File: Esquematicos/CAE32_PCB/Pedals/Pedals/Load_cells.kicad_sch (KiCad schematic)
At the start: 51 parts, among them J17 Conn_01x07_Female, J18 Conn_01x07_Female, J19 Conn_01x07_Female, Q1 MMBT3906, Q2 MMBT3906, Q3 MMBT3906, U5 HX711, U6 HX711, U7 HX711

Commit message: update: Componentes acomodados en la PCB
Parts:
- J18: renamed from J17; value Conn_01x07_Female -> LC_2
- J19: renamed from J18; value Conn_01x07_Female -> LD_1
- J20: renamed from J19; value Conn_01x07_Female -> LC_3
- R10, R11, R12, R13, R14, R15, R16, R17, R18, R19, R20, R6, R7, R8, R9: footprint Resistor_SMD:R_0805_2012Metric_Pad1.20x1.40mm_HandSolder -> Resistor_SMD:R_0603_1608Metric_Pad0.98x0.95mm_HandSolder
- renumbered C23 to C15, C24 to C16, C25 to C17, C26 to C18, C15 to C19, C27 to C20, C28 to C21, C16 to C22, C17 to C23, C18 to C24, C19 to C25, C20 to C26, C21 to C27, C22 to C28, C33 to C29, C34 to C30, C29 to C31, C35 to C32, C30 to C33, C31 to C34, C32 to C35
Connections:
- net B2+: no longer J20.2 (Pin_2)
- net B3+: now also J20.2 (Pin_2)
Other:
- moved on the sheet: C15, C16, C17, C18, C19, C20, C21, C23, C25, C27, C29, C30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

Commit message: update: se agrega el consumo de corriente a los IC's ademas de agregar el URL y numero de parte de los componentes de LCSC en kicad
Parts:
- C15, C16, C17, C18, C19, C22, C23, C24, C27, C28, C29, C30, C31, C33, C35: value 0u1 -> 100n; LCSC_PART (none) -> c1591
- C20, C21, C25, C26, C32, C34: LCSC_PART (none) -> C1691
- J18, J20: LCSC_PART (none) -> C2832270
- J19: value LD_1 -> LC_1; LCSC_PART (none) -> C2832270
- L1, L2, L3: LCSC_PART (none) -> C84474
- R10, R12, R18: LCSC_PART (none) -> C4184
- R11, R13, R19: LCSC_PART (none) -> C114637
- R14, R15, R20: LCSC_PART (none) -> C25804
- R16, R17, R6, R7, R8, R9: LCSC_PART (none) -> C22775
- U5, U6, U7: LCSC_PART (none) -> C43656
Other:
- note added: "ANALOG SUPPLY CURRENT: 1400uA DIGITAL SUPPLY CURRENT: 100uA"
- note added: "HX711"
- title: (none) -> CAE32 pedals

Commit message: Update: esquematicos de PCB, reorganizando elementos para hacer mas compacta la pcb, ademas de agregar serigrafia e imagenes de la PCB
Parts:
- added TP4, TP5, TP6, TP7: TestPoint, TestPoint:TestPoint_Pad_D1.0mm, symbol Connector:TestPoint
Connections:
- net DOUT_1: now also TP5.1
- net DOUT_2: now also TP4.1
- net DOUT_3: now also TP7.1
- net PD_SCK: now also TP6.1
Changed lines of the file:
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@@
   (junction (at 71.12 123.19) (diameter 0) (color 0 0 0 0)
   )
+  (junction (at 118.745 46.355) (diameter 0) (color 0 0 0 0)
+  )
   (junction (at 195.58 87.63) (diameter 0) (color 0 0 0 0)
   )
@@
   (junction (at 73.025 34.925) (diameter 0) (color 0 0 0 0)
   )
+  (junction (at 133.985 48.895) (diameter 0) (color 0 0 0 0)
+  )
+  (junction (at 258.445 99.06) (diameter 0) (color 0 0 0 0)
+  )
   (junction (at 45.72 123.19) (diameter 0) (color 0 0 0 0)
   )
@@
   )
   (junction (at 71.12 132.08) (diameter 0) (color 0 0 0 0)
+  )
+  (junction (at 117.475 134.62) (diameter 0) (color 0 0 0 0)
   )
   (junction (at 51.435 130.81) (diameter 0) (color 0 0 0 0)
@@
     (stroke (width 0) (type default) (color 0 0 0 0))
   )
+  (wire (pts (xy 264.16 99.06) (xy 258.445 99.06))
+    (stroke (width 0) (type default) (color 0 0 0 0))
+  )
   (wire (pts (xy 227.33 99.06) (xy 223.52 99.06))
     (stroke (width 0) (type default) (color 0 0 0 0))
@@
     (stroke (width 0) (type default) (color 0 0 0 0))
   )
+  (wire (pts (xy 123.19 46.355) (xy 118.745 46.355))
+    (stroke (width 0) (type default) (color 0 0 0 0))
+  )
   (polyline (pts (xy 20.955 52.705) (xy 31.115 52.705))
     (stroke (width 0.5) (type solid) (color 255 132 74 1))
@@
     (stroke (width 0) (type default) (color 0 0 0 0))
   )
+  (wire (pts (xy 116.205 48.895) (xy 133.985 48.895))
+    (stroke (width 0) (type default) (color 0 0 0 0))
+  )
   (wire (pts (xy 87.63 132.08) (xy 88.9 132.08))
     (stroke (width 0) (type default) (color 0 0 0 0))
@@
   )
   (wire (pts (xy 73.025 33.655) (xy 73.025 34.925))
+    (stroke (width 0) (type default) (color 0 0 0 0))
+  )
+  (wire (pts (xy 258.445 99.06) (xy 252.73 99.06))
     (stroke (width 0) (type default) (color 0 0 0 0))
   )
@@
     (stroke (width 0) (type default) (color 0 0 0 0))
   )
+  (wire (pts (xy 118.745 46.355) (xy 116.205 46.355))
+    (stroke (width 0) (type default) (color 0 0 0 0))
+  )
   (wire (pts (xy 90.805 28.575) (xy 90.805 41.275))
     (stroke (width 0) (type default) (color 0 0 0 0))
@@
     (stroke (width 0) (type default) (color 0 0 0 0))
   )
+  (wire (pts (xy 117.475 134.62) (xy 119.38 134.62))
+    (stroke (width 0) (type default) (color 0 0 0 0))
+  )
+  (wire (pts (xy 133.985 48.895) (xy 135.89 48.895))
+    (stroke (width 0) (type default) (color 0 0 0 0))
+  )
   (wire (pts (xy 71.12 130.81) (xy 71.12 132.08))
     (stroke (width 0) (type default) (color 0 0 0 0))
@@
   (polyline (pts (xy 31.115 52.705) (xy 31.115 33.655))
     (stroke (width 0.5) (type solid) (color 255 132 74 1))
+  )
+  (wire (pts (xy 114.3 134.62) (xy 117.475 134.62))
+    (stroke (width 0) (type default) (color 0 0 0 0))
   )
   (wire (pts (xy 51.435 130.81) (xy 51.435 131.445))
@@
     (effects (font (size 1.27 1.27)) (justify left))
   )
-  (hierarchical_label "PD_SCK" (shape input) (at 116.205 48.895 0)
+  (hierarchical_label "PD_SCK" (shape input) (at 135.89 48.895 0)
     (effects (font (size 1.27 1.27)) (justify left))
   )
-  (hierarchical_label "DOUT_3" (shape output) (at 252.73 99.06 0)
+  (hierarchical_label "DOUT_3" (shape output) (at 264.16 99.06 0)
     (effects (font (size 1.27 1.27)) (justify left))
   )
-  (hierarchical_label "DOUT_1" (shape output) (at 116.205 46.355 0)
+  (hierarchical_label "DOUT_1" (shape output) (at 123.19 46.355 0)
     (effects (font (size 1.27 1.27)) (justify left))
   )
@@
     (effects (font (size 1.27 1.27)) (justify left))
   )
-  (hierarchical_label "DOUT_2" (shape output) (at 114.3 134.62 0)
+  (hierarchical_label "DOUT_2" (shape output) (at 119.38 134.62 0)
     (effects (font (size 1.27 1.27)) (justify left))
   )
@@
     )
     (property "Datasheet" "" (id 3) (at 53.975 45.085 0)
+      (effects (font (size 1.27 1.27)) hide)
+    )
+    (pin "1")
+  )
+  (symbol (lib_id "Connector:TestPoint") (at 258.445 99.06 0) (unit 1)
+    (in_bom yes) (on_board yes) (fields_autoplaced)
+    (property "Reference" "TP7" (id 0) (at 260.35 94.4879 0)
+      (effects (font (size 1.27 1.27)) (justify left))
+    )
+    (property "Value" "TestPoint" (id 1) (at 260.35 97.0279 0)
+      (effects (font (size 1.27 1.27)) (justify left))
+    )
+    (property "Footprint" "TestPoint:TestPoint_Pad_D1.0mm" (id 2) (at 263.525 99.06 0)
+      (effects (font (size 1.27 1.27)) hide)
+    )
+    (property "Datasheet" "~" (id 3) (at 263.525 99.06 0)
       (effects (font (size 1.27 1.27)) hide)
     )
@@
     (pin "1")
   )
+  (symbol (lib_id "Connector:TestPoint") (at 118.745 46.355 0) (unit 1)
+    (in_bom yes) (on_board yes) (fields_autoplaced)
+    (property "Reference" "TP5" (id 0) (at 120.65 41.7829 0)
+      (effects (font (size 1.27 1.27)) (justify left))
+    )
+    (property "Value" "TestPoint" (id 1) (at 120.65 44.3229 0)
+      (effects (font (size 1.27 1.27)) (justify left))
+    )
+    (property "Footprint" "TestPoint:TestPoint_Pad_D1.0mm" (id 2) (at 123.825 46.355 0)
+      (effects (font (size 1.27 1.27)) hide)
+    )
+    (property "Datasheet" "~" (id 3) (at 123.825 46.355 0)
+      (effects (font (size 1.27 1.27)) hide)
+    )
+    (pin "1")
+  )
   (symbol (lib_id "Jumper:SolderJumper_2_Open") (at 120.65 156.21 90) (unit 1)
     (in_bom yes) (on_board yes) (fields_autoplaced)
@@
     (pin "1")
     (pin "2")
+  )
+  (symbol (lib_id "Connector:TestPoint") (at 133.985 48.895 0) (unit 1)
+    (in_bom yes) (on_board yes) (fields_autoplaced)
+    (property "Reference" "TP6" (id 0) (at 135.89 44.3229 0)
+      (effects (font (size 1.27 1.27)) (justify left))
+    )
+    (property "Value" "TestPoint" (id 1) (at 135.89 46.8629 0)
+      (effects (font (size 1.27 1.27)) (justify left))
+    )
+    (property "Footprint" "TestPoint:TestPoint_Pad_D1.0mm" (id 2) (at 139.065 48.895 0)
+      (effects (font (size 1.27 1.27)) hide)
+    )
+    (property "Datasheet" "~" (id 3) (at 139.065 48.895 0)
+      (effects (font (size 1.27 1.27)) hide)
+    )
+    (pin "1")
   )
   (symbol (lib_id "Transistor_BJT:MMBT3906") (at 212.09 81.28 180) (unit 1)
@@
     (pin "3")
   )
+  (symbol (lib_id "Connector:TestPoint") (at 117.475 134.62 0) (unit 1)
+    (in_bom yes) (on_board yes) (fields_autoplaced)
+    (property "Reference" "TP4" (id 0) (at 119.38 130.0479 0)
+      (effects (font (size 1.27 1.27)) (justify left))
+    )
+    (property "Value" "TestPoint" (id 1) (at 119.38 132.5879 0)
+      (effects (font (size 1.27 1.27)) (justify left))
+    )
+    (property "Footprint" "TestPoint:TestPoint_Pad_D1.0mm" (id 2) (at 122.555 134.62 0)
+      (effects (font (size 1.27 1.27)) hide)
+    )
+    (property "Datasheet" "~" (id 3) (at 122.555 134.62 0)
+      (effects (font (size 1.27 1.27)) hide)
+    )
+    (pin "1")
+  )
   (symbol (lib_id "Device:R_Small_US") (at 48.26 154.94 270) (unit 1)

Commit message: update: se crea la primera revisión de la PCB
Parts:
- C15, C16, C17, C18, C19, C22, C23, C24, C27, C28, C29, C30, C31, C33, C35: Item (none) -> c1591; Qty (none) -> 22; Vendor (none) -> c1591
- C20, C21, C25, C26, C32, C34: Item (none) -> C1691; Qty (none) -> 6; Vendor (none) -> C1691
- J18, J19, J20: Item (none) -> C2832270; Qty (none) -> 1; Vendor (none) -> C2832270
- JP1, JP2, JP3, Q1, Q2, Q3: Qty (none) -> 3
- L1, L2, L3: Item (none) -> C84474; Qty (none) -> 3; Vendor (none) -> C84474
- R10: renamed from R8; Item (none) -> C22775; Qty (none) -> 6; Vendor (none) -> C22775
- R11: renamed from R9; Item (none) -> C22775; Qty (none) -> 6; Vendor (none) -> C22775
- R12: renamed from R10; Item (none) -> C4184; Qty (none) -> 3; Vendor (none) -> C4184
- R13: renamed from R11; Item (none) -> C114637; Qty (none) -> 3; Vendor (none) -> C114637
- R14: renamed from R12; Item (none) -> C4184; Qty (none) -> 3; Vendor (none) -> C4184
- R15: renamed from R13; Item (none) -> C114637; Qty (none) -> 3; Vendor (none) -> C114637
- R16: renamed from R14; Item (none) -> C25804; Qty (none) -> 3; Vendor (none) -> C25804
- R17: renamed from R15; Item (none) -> C25804; Qty (none) -> 3; Vendor (none) -> C25804
- R18: renamed from R16; Item (none) -> C22775; Qty (none) -> 6; Vendor (none) -> C22775
- R19: renamed from R17; Item (none) -> C22775; Qty (none) -> 6; Vendor (none) -> C22775
- R20: renamed from R18; Item (none) -> C4184; Qty (none) -> 3; Vendor (none) -> C4184
- R21: renamed from R19; Item (none) -> C114637; Qty (none) -> 3; Vendor (none) -> C114637
- R22: renamed from R20; Item (none) -> C25804; Qty (none) -> 3; Vendor (none) -> C25804
- R8: renamed from R6; Item (none) -> C22775; Qty (none) -> 6; Vendor (none) -> C22775
- R9: renamed from R7; Item (none) -> C22775; Qty (none) -> 6; Vendor (none) -> C22775
- TP4, TP5, TP6, TP7: Qty (none) -> 4
- U5, U6, U7: Item (none) -> C43656; Qty (none) -> 3; Vendor (none) -> C43656

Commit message: add: plantilla para diseño de pcb para shifter
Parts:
- Q1, Q2, Q3: Vendor (none) -> C2891809
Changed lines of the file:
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@@
+      (effects (font (size 1.27 1.27)) hide)
+    )
+    (property "Vendor" "C2891809" (id 5) (at 75.565 28.575 0)
       (effects (font (size 1.27 1.27)) hide)
     )
@@
       (effects (font (size 1.27 1.27)) hide)
     )
+    (property "Vendor" "C2891809" (id 5) (at 212.09 81.28 0)
+      (effects (font (size 1.27 1.27)) hide)
+    )
     (pin "1")
     (pin "2")
@@
       (effects (font (size 1.27 1.27)) hide)
     )
+    (property "Vendor" "C2891809" (id 5) (at 73.66 116.84 0)
+      (effects (font (size 1.27 1.27)) hide)
+    )

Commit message: chore: arrange schematics components
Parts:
- C15, C16, C17, C18, C19, C20, C21, C22, C23, C24, C25, C26, C27, C28, C29, C30, C31, C32, C33, C34, C35: footprint Capacitor_SMD:C_0603_1608Metric_Pad1.08x0.95mm_HandSolder -> Capacitor_SMD:C_0603_1608Metric
- L1, L2, L3: footprint Inductor_SMD:L_0402_1005Metric_Pad0.77x0.64mm_HandSolder -> Inductor_SMD:L_0402_1005Metric
- R10, R11, R12, R13, R14, R15, R16, R17, R18, R19, R20, R21, R22, R8, R9: footprint Resistor_SMD:R_0603_1608Metric_Pad0.98x0.95mm_HandSolder -> Resistor_SMD:R_0603_1608Metric

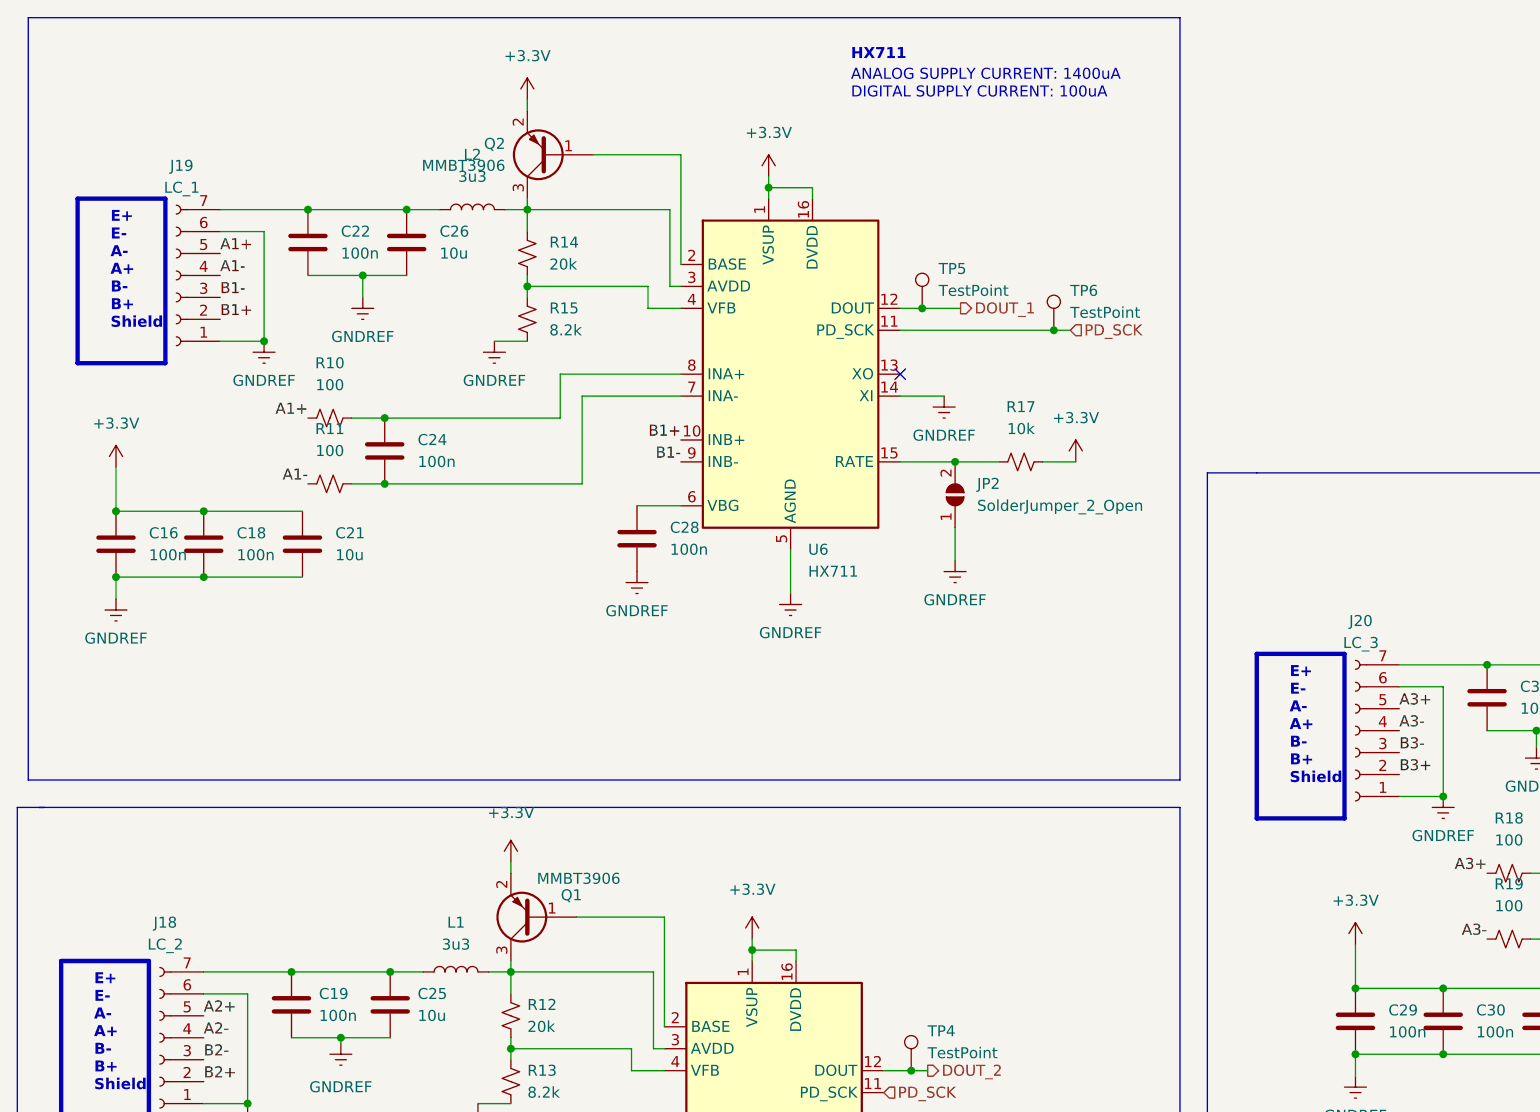
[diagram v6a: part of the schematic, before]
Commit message: update: added minor improvements to Pedal's PCB
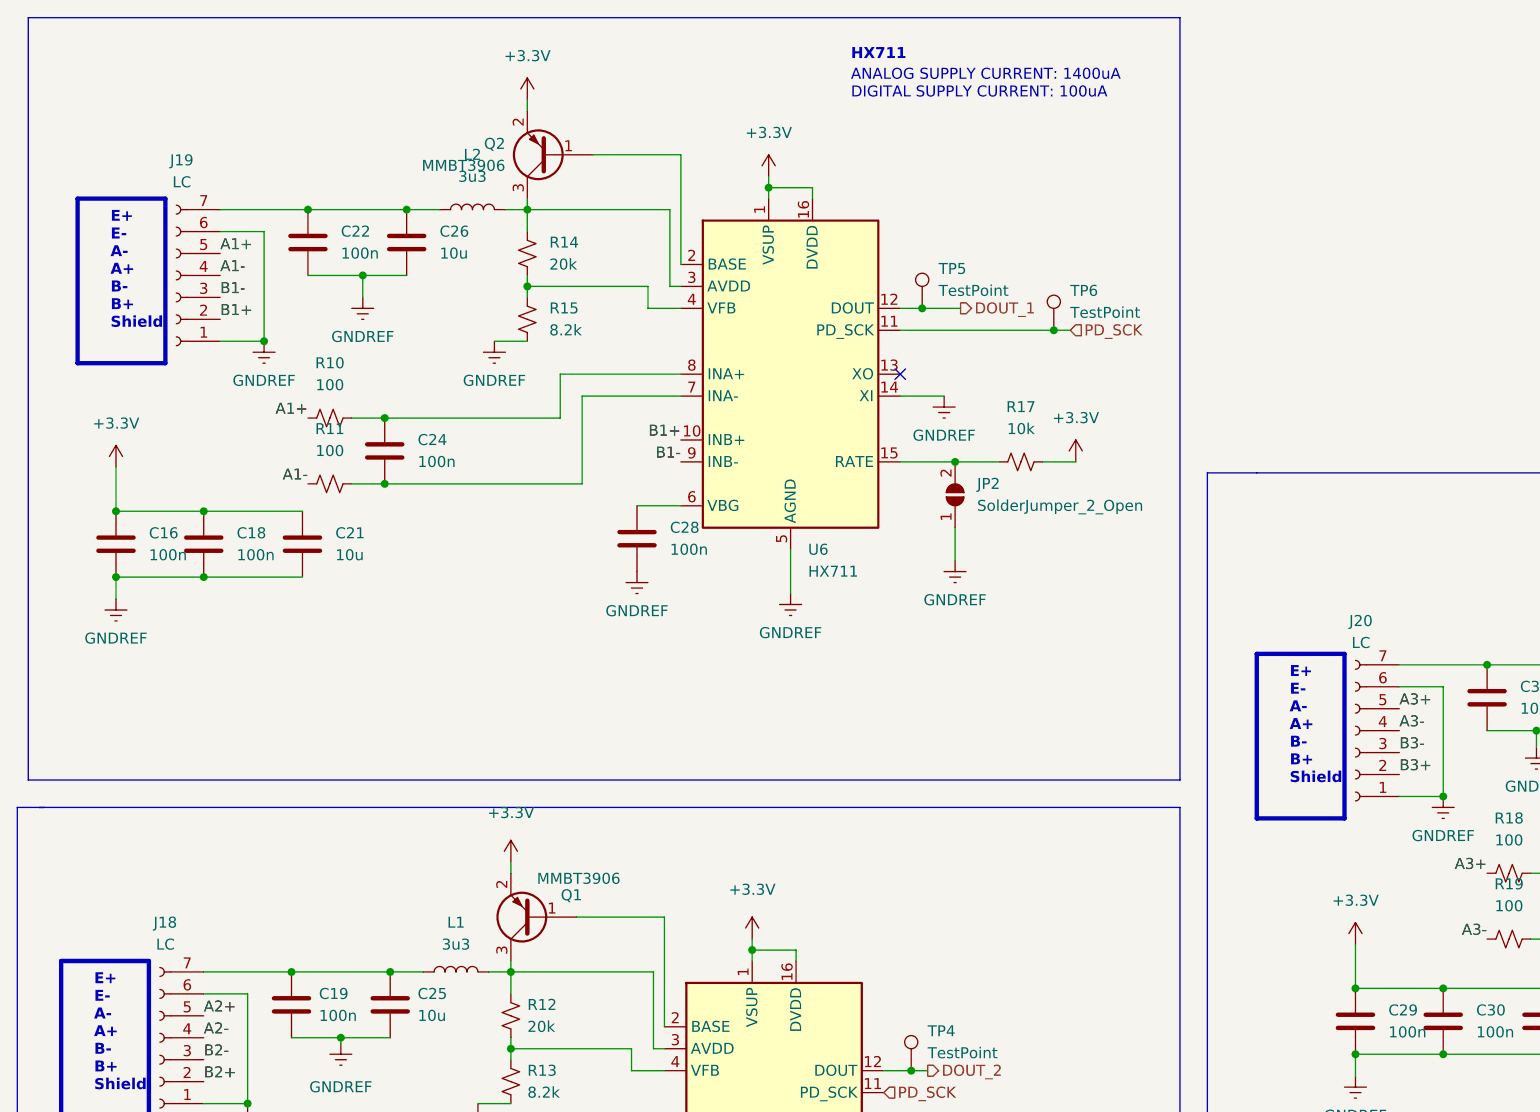
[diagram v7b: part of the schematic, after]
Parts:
- J18: value LC_2 -> LC
- J19: value LC_1 -> LC
- J20: value LC_3 -> LC
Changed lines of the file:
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@@
       (effects (font (size 1.27 1.27)))
     )
-    (property "Value" "LC_3" (at 169.545 85.09 0)
+    (property "Value" "LC" (at 169.545 85.09 0)
       (effects (font (size 1.27 1.27)))
     )
@@
       (effects (font (size 1.27 1.27)))
     )
-    (property "Value" "LC_2" (at 31.115 120.015 0)
+    (property "Value" "LC" (at 31.115 120.015 0)
       (effects (font (size 1.27 1.27)))
     )
@@
   (symbol (lib_id "Connector:Conn_01x07_Female") (at 32.385 42.545 180) (unit 1)
     (in_bom yes) (on_board yes) (dnp no) (fields_autoplaced)
-    (property "Reference" "J19" (at 33.02 29.845 0)
-      (effects (font (size 1.27 1.27)))
-    )
-    (property "Value" "LC_1" (at 33.02 32.385 0)
-      (effects (font (size 1.27 1.27)))
-    )
+    (property "Reference" "J19" (at 33.02 29.21 0)
+      (effects (font (size 1.27 1.27)))
+    )
+    (property "Value" "LC" (at 33.02 31.75 0)
+      (effects (font (size 1.27 1.27)))
+    )

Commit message: update: PCB pedals Version:2.1.1
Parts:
- removed J18, J19, J20: LC, Connector_PinSocket_2.54mm:PinSocket_1x07_P2.54mm_Vertical, symbol Connector:Conn_01x07_Female
- added J17, J18, J19: LC, TerminalBlock_TE-Connectivity:TerminalBlock_TE_282834-7_1x07_P2.54mm_Horizontal, symbol Connector:Screw_Terminal_01x07
- R10, R11, R18, R19, R8, R9: Item C22775 -> C25201; LCSC_PART C22775 -> C25201; Qty 6 -> 14; Vendor C22775 -> C25201
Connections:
- net A1+: now also J17.5 (Pin_5)
- net A1-: now also J17.4 (Pin_4)
- net A2+: now also J19.5 (Pin_5)
- net A2-: now also J19.4 (Pin_4)
- net A3+: now also J18.5 (Pin_5)
- net A3-: now also J18.4 (Pin_4)
- net B1+: now also J17.2 (Pin_2)
- net B1-: now also J17.3 (Pin_3)
- net B2+: now also J19.2 (Pin_2)
- net B2-: now also J19.3 (Pin_3)
- net B3+: now also J18.2 (Pin_2)
- net B3-: now also J18.3 (Pin_3)
- net GNDREF: now also J17.1 (Pin_1), J17.6 (Pin_6), J18.1 (Pin_1), J18.6 (Pin_6), J19.1 (Pin_1), J19.6 (Pin_6)
- net at C31.1, C34.1, L3.1: now also J18.7 (Pin_7)
- net at C19.1, C25.1, L1.1: now also J19.7 (Pin_7)
- net at C22.1, C26.1, L2.1: now also J17.7 (Pin_7)
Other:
- note added: "E+ E- A+ A- B- B+ Shield"
- note removed: "E+ E- A- A+ B- B+ Shield"
